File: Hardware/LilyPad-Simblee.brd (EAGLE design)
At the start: 45.3 x 45.2 mm, 36 parts, among them U1 MIC5219 3.3V, U2 MCP73831, U3 RFD77101

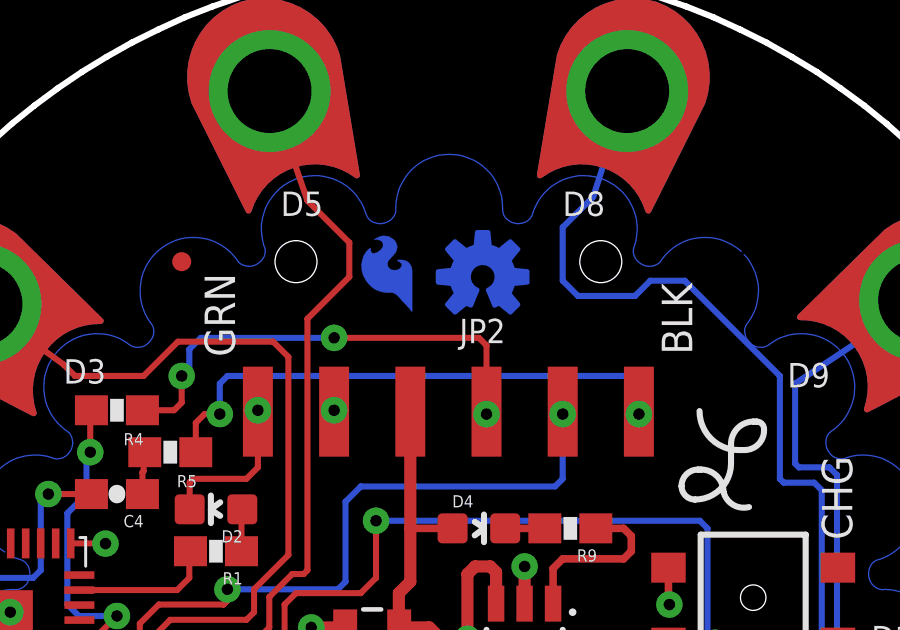
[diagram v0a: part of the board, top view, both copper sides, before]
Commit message: Fixed QC feedback issues.
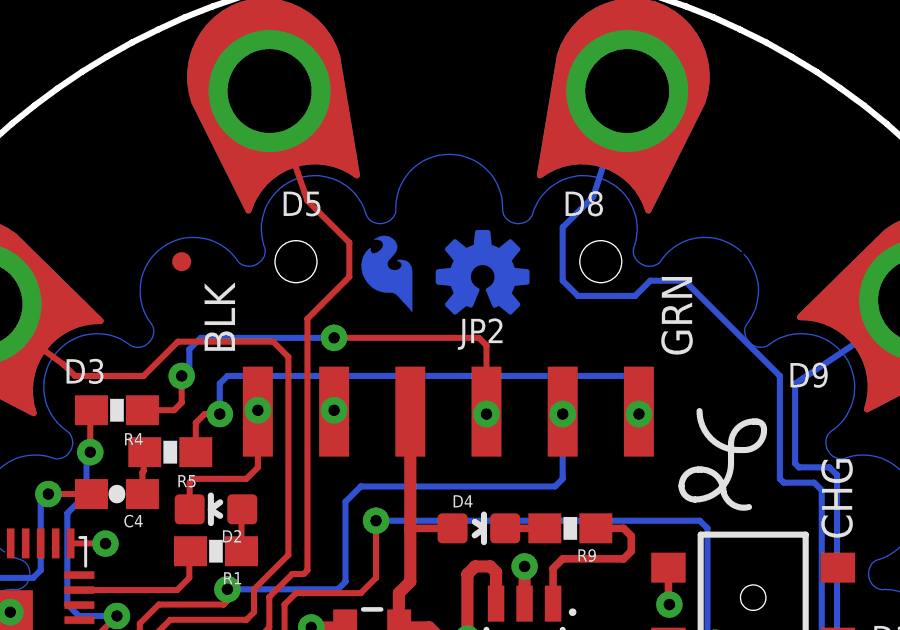
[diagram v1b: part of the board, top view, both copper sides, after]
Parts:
- added U$2: LOGO-LPLP, LilyPad-Wearables:LOGO-LILYPAD
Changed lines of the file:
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@@
 <grid distance="0.05" unitdist="inch" unit="inch" style="lines" multiple="1" display="yes" altdistance="0.005" altunitdist="inch" altunit="inch"/>
 <layers>
-<layer number="1" name="Top" color="4" fill="1" visible="yes" active="yes"/>
-<layer number="2" name="Route2" color="1" fill="3" visible="yes" active="yes"/>
-<layer number="15" name="Route15" color="4" fill="6" visible="yes" active="yes"/>
+<layer number="1" name="Top" color="4" fill="1" visible="no" active="yes"/>
+<layer number="2" name="Route2" color="1" fill="3" visible="no" active="yes"/>
+<layer number="15" name="Route15" color="4" fill="6" visible="no" active="yes"/>
 <layer number="16" name="Bottom" color="1" fill="1" visible="yes" active="yes"/>
 <layer number="17" name="Pads" color="2" fill="1" visible="yes" active="yes"/>
@@
 <layer number="19" name="Unrouted" color="6" fill="1" visible="yes" active="yes"/>
 <layer number="20" name="Dimension" color="6" fill="1" visible="yes" active="yes"/>
-<layer number="21" name="tPlace" color="16" fill="1" visible="yes" active="yes"/>
+<layer number="21" name="tPlace" color="16" fill="1" visible="no" active="yes"/>
 <layer number="22" name="bPlace" color="14" fill="1" visible="yes" active="yes"/>
-<layer number="23" name="tOrigins" color="15" fill="1" visible="yes" active="yes"/>
+<layer number="23" name="tOrigins" color="15" fill="1" visible="no" active="yes"/>
 <layer number="24" name="bOrigins" color="15" fill="1" visible="yes" active="yes"/>
-<layer number="25" name="tNames" color="7" fill="1" visible="yes" active="yes"/>
-<layer number="26" name="bNames" color="7" fill="1" visible="yes" active="yes"/>
-<layer number="27" name="tValues" color="7" fill="1" visible="yes" active="yes"/>
-<layer number="28" name="bValues" color="7" fill="1" visible="yes" active="yes"/>
-<layer number="29" name="tStop" color="5" fill="1" visible="yes" active="yes"/>
+<layer number="25" name="tNames" color="7" fill="1" visible="no" active="yes"/>
+<layer number="26" name="bNames" color="7" fill="1" visible="no" active="yes"/>
+<layer number="27" name="tValues" color="7" fill="1" visible="no" active="yes"/>
+<layer number="28" name="bValues" color="7" fill="1" visible="no" active="yes"/>
+<layer number="29" name="tStop" color="5" fill="1" visible="no" active="yes"/>
 <layer number="30" name="bStop" color="7" fill="6" visible="yes" active="yes"/>
-<layer number="31" name="tCream" color="7" fill="4" visible="yes" active="yes"/>
-<layer number="32" name="bCream" color="7" fill="5" visible="yes" active="yes"/>
-<layer number="39" name="tKeepout" color="4" fill="11" visible="yes" active="yes"/>
-<layer number="40" name="bKeepout" color="1" fill="11" visible="yes" active="yes"/>
-<layer number="41" name="tRestrict" color="4" fill="10" visible="yes" active="yes"/>
-<layer number="42" name="bRestrict" color="1" fill="10" visible="yes" active="yes"/>
-<layer number="43" name="vRestrict" color="2" fill="10" visible="yes" active="yes"/>
-<layer number="44" name="Drills" color="7" fill="1" visible="yes" active="yes"/>
-<layer number="45" name="Holes" color="7" fill="1" visible="yes" active="yes"/>
-<layer number="46" name="Milling" color="3" fill="1" visible="yes" active="yes"/>
+<layer number="31" name="tCream" color="7" fill="4" visible="no" active="yes"/>
+<layer number="32" name="bCream" color="7" fill="5" visible="no" active="yes"/>
+<layer number="39" name="tKeepout" color="4" fill="11" visible="no" active="yes"/>
+<layer number="40" name="bKeepout" color="1" fill="11" visible="no" active="yes"/>
+<layer number="41" name="tRestrict" color="4" fill="10" visible="no" active="yes"/>
+<layer number="42" name="bRestrict" color="1" fill="10" visible="no" active="yes"/>
+<layer number="43" name="vRestrict" color="2" fill="10" visible="no" active="yes"/>
+<layer number="44" name="Drills" color="7" fill="1" visible="no" active="yes"/>
+<layer number="45" name="Holes" color="7" fill="1" visible="no" active="yes"/>
+<layer number="46" name="Milling" color="3" fill="1" visible="no" active="yes"/>
 <layer number="47" name="Measures" color="7" fill="1" visible="yes" active="yes"/>
-<layer number="51" name="tDocu" color="6" fill="1" visible="yes" active="yes"/>
+<layer number="51" name="tDocu" color="6" fill="1" visible="no" active="yes"/>
 <layer number="3" name="Route3" color="4" fill="3" visible="no" active="no"/>
 <layer number="4" name="Route4" color="1" fill="4" visible="no" active="no"/>
@@
 <text x="13.462" y="-4.191" size="1.016" layer="21" font="vector" ratio="15" rot="R90" align="bottom-center">ON</text>
 <text x="12.446" y="4.826" size="1.016" layer="21" font="vector" ratio="15" rot="R90" align="top-center">CHG</text>
-<text x="7.112" y="10.795" size="1.016" layer="21" font="vector" ratio="15" rot="R90" align="top-center">BLK</text>
-<text x="-7.112" y="10.922" size="1.016" layer="21" font="vector" ratio="15" rot="R90" align="bottom-center">GRN</text>
+<text x="-8.128" y="10.795" size="1.016" layer="21" font="vector" ratio="15" rot="R90" align="top-center">BLK</text>
+<text x="8.128" y="10.922" size="1.016" layer="21" font="vector" ratio="15" rot="R90" align="bottom-center">GRN</text>
 <wire x1="0.0264" y1="-0.003875" x2="0.0264" y2="26.816125" width="0.127" layer="51"/>
 <wire x1="0.0264" y1="-0.003875" x2="-8.2636" y2="25.496125" width="0.127" layer="51"/>
@@
 <text x="22.86" y="-24.13" size="1.778" layer="51" font="vector" ratio="15">NOTE: Use 0.32" board thickness!</text>
 <text x="73.66" y="-31.75" size="1.778" layer="51" font="vector" ratio="15">Mike Hord</text>
-<dimension x1="0" y1="22.86" x2="0" y2="-22.86" x3="-34.29" y3="0" textsize="1.778" textratio="15" layer="51" dtype="vertical" unit="inch"/>
+<dimension x1="0" y1="22.86" x2="0" y2="-22.86" x3="-34.29" y3="0" textsize="1.778" textratio="15" layer="47" dtype="vertical" unit="inch"/>
+<circle x="0" y="-2.667" radius="0.508" width="0" layer="47"/>
 </plain>
 <attributes>
@@
 <element name="FID2" library="SparkFun-Aesthetics" package="MICRO-FIDUCIAL" value="FIDUCIALUFIDUCIAL" x="8.89" y="-12.319"/>
 <element name="U$1" library="LilyPad-Wearables" package="LOGO-L" value="LOGO-LPL" x="9.144" y="6.096"/>
+<element name="U$2" library="LilyPad-Wearables" package="LOGO-LILYPAD" value="LOGO-LPLP" x="0.127" y="0.381" rot="MR0"/>
 </elements>
 <signals>
